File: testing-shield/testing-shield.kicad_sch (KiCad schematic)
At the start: 30 parts, among them J1 I2C Grove, J2 I2C Socket, J3 I2C Header, J4 Side SPI, J5 ISP SPI, J6 UART Header, J7 UART Grove, SW1 UART, SW2 Side SPI, SW3 ISP SPI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

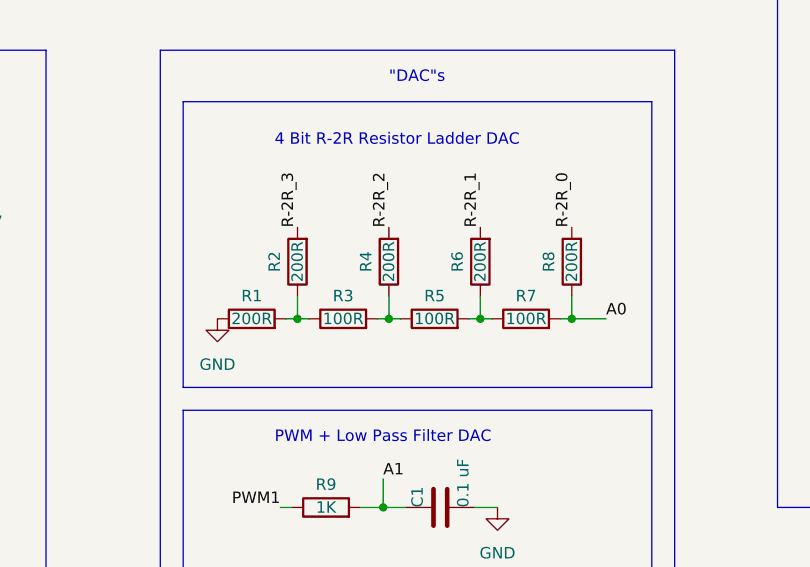
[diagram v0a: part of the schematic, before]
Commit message: testing-shield: Fix R-2R DAC resistor values
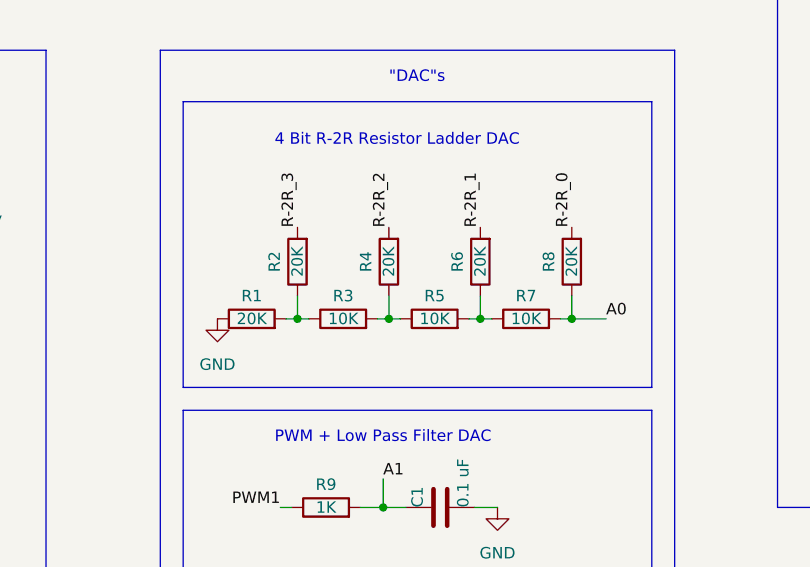
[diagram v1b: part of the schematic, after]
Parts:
- R1, R2, R4, R6, R8: value 200R -> 20K
- R3, R5, R7: value 100R -> 10K
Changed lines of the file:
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@@
       (effects (font (size 1.27 1.27)))
     )
-    (property "Value" "200R" (at 130.81 136.525 90)
+    (property "Value" "20K" (at 130.81 136.525 90)
       (effects (font (size 1.27 1.27)))
     )
@@
       (effects (font (size 1.27 1.27)))
     )
-    (property "Value" "100R" (at 146.05 142.875 90)
+    (property "Value" "10K" (at 146.05 142.875 90)
       (effects (font (size 1.27 1.27)))
     )
@@
       (effects (font (size 1.27 1.27)))
     )
-    (property "Value" "200R" (at 140.97 136.525 90)
+    (property "Value" "20K" (at 140.97 136.525 90)
       (effects (font (size 1.27 1.27)))
     )
@@
       (effects (font (size 1.27 1.27)))
     )
-    (property "Value" "100R" (at 135.89 142.875 90)
+    (property "Value" "10K" (at 135.89 142.875 90)
       (effects (font (size 1.27 1.27)))
     )
@@
       (effects (font (size 1.27 1.27)))
     )
-    (property "Value" "100R" (at 156.21 142.875 90)
+    (property "Value" "10K" (at 156.21 142.875 90)
       (effects (font (size 1.27 1.27)))
     )
@@
       (effects (font (size 1.27 1.27)))
     )
-    (property "Value" "200R" (at 151.13 136.525 90)
+    (property "Value" "20K" (at 151.13 136.525 90)
       (effects (font (size 1.27 1.27)))
     )
@@
       (effects (font (size 1.27 1.27)))
     )
-    (property "Value" "200R" (at 161.29 136.525 90)
+    (property "Value" "20K" (at 161.29 136.525 90)
       (effects (font (size 1.27 1.27)))
     )
@@
       (effects (font (size 1.27 1.27)))
     )
-    (property "Value" "200R" (at 125.73 142.875 90)
-      (effects (font (size 1.27 1.27)))
-    )
+    (property "Value" "20K" (at 125.73 142.875 90)
+      (effects (font (size 1.27 1.27)))
+    )

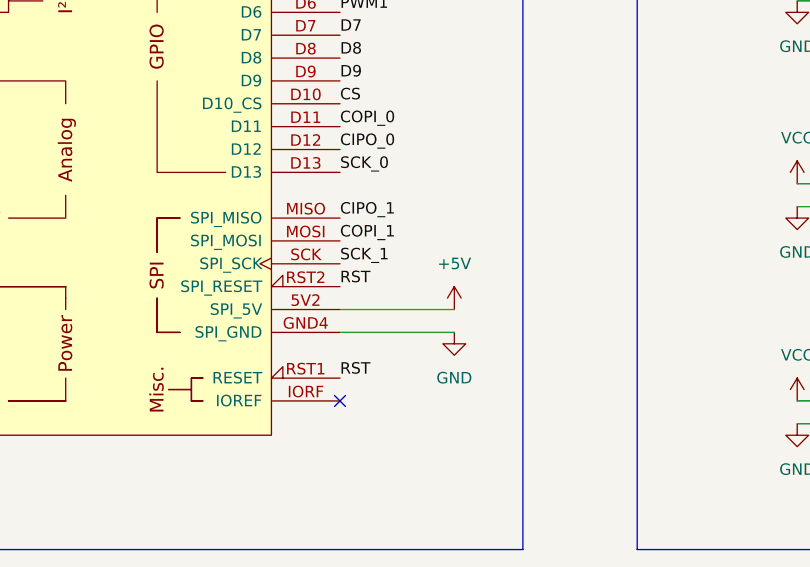
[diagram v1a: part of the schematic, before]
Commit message: testing-shield: do not connect to 5V pin of ISP
Some boards (e.g. the Seeeduino) do not have 5V but VCC there.
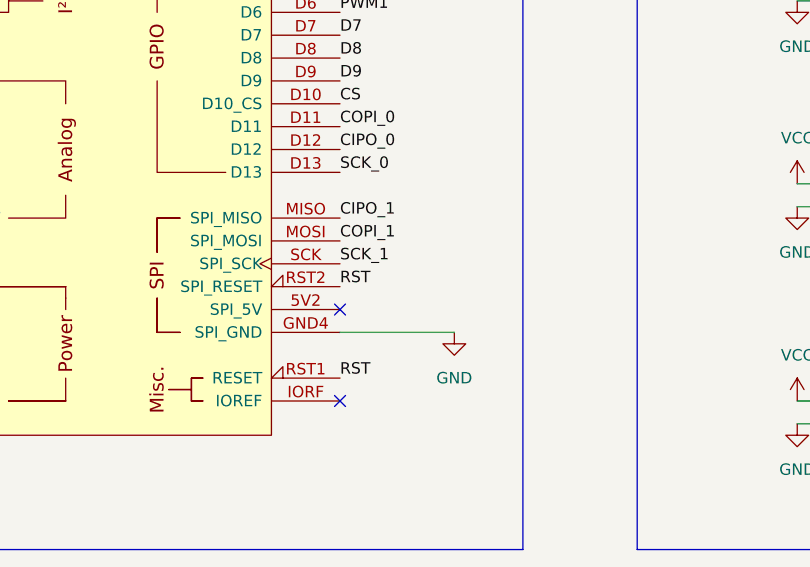
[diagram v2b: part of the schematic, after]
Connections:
- net +5V: no longer XA1.5V2 (SPI_5V)
- no-connect marks 3 -> 4
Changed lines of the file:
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@@
   (junction (at 29.21 85.09) (diameter 0) (color 0 0 0 0)
   )
+  (no_connect (at 82.55 77.47))
   (no_connect (at 31.75 67.31))
   (no_connect (at 82.55 87.63))
@@
   )
   (wire (pts (xy 151.13 142.875) (xy 152.4 142.875))
-    (stroke (width 0) (type default))
-  )
-  (wire (pts (xy 82.55 77.47) (xy 95.25 77.47))
     (stroke (width 0) (type default))
   )
@@
         )
       )
-    )
-  )
-  (symbol (lib_id "power:+5V") (at 95.25 77.47 0) (unit 1)
-    (in_bom yes) (on_board yes) (dnp no) (fields_autoplaced)
-    (property "Reference" "#PWR04" (at 95.25 81.28 0)
-      (effects (font (size 1.27 1.27)) hide)
-    )
-    (property "Value" "+5V" (at 95.25 72.39 0)
-      (effects (font (size 1.27 1.27)))
-    )
-    (property "Footprint" "" (at 95.25 77.47 0)
-      (effects (font (size 1.27 1.27)) hide)
-    )
-    (property "Datasheet" "" (at 95.25 77.47 0)
-      (effects (font (size 1.27 1.27)) hide)
-    )
-    (pin "1")
-    (instances
-      (project "testing-shield"
-        (path "/e57ba8ab-33c5-4264-a7ca-fe36cd423955"
-          (reference "#PWR04") (unit 1)
-        )
-      )

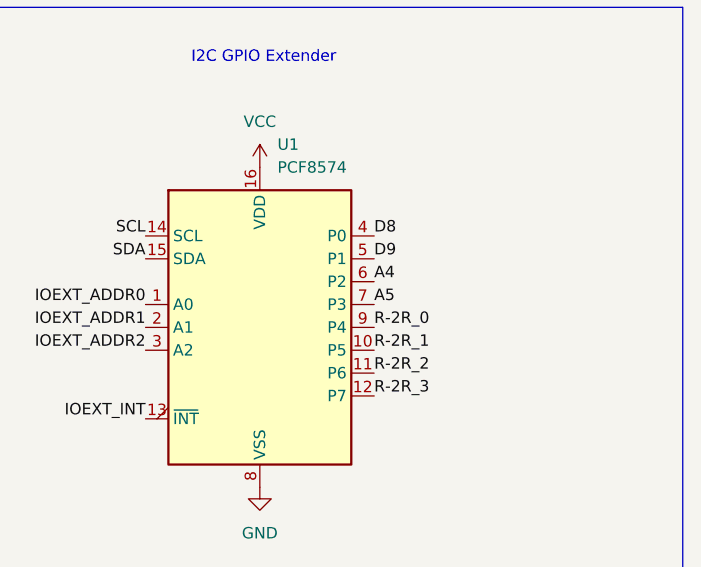
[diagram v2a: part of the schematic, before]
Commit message: testing-shield: connect SCK lines to GPIO extender
This allows reading the SPI clock polarity when the SPI clock is
idle.
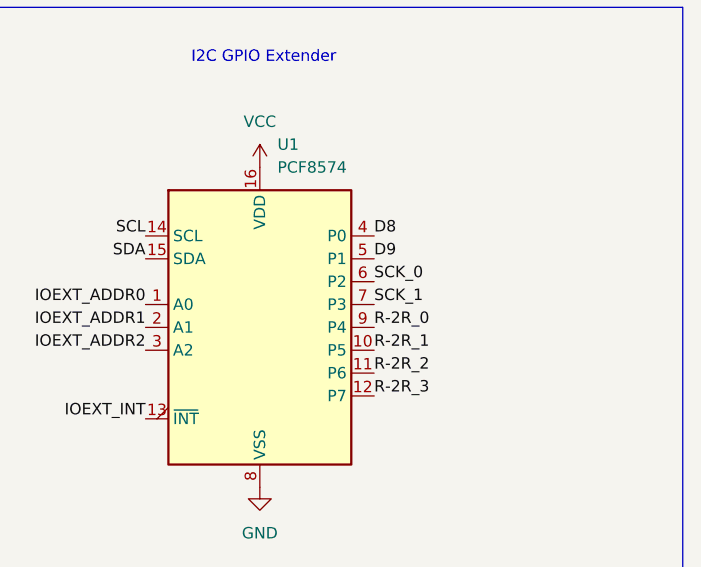
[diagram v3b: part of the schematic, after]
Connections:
- net A4: no longer U1.6 (P2)
- net A5: no longer U1.7 (P3)
- net SCK_0: now also U1.6 (P2)
- net SCK_1: now also U1.7 (P3)
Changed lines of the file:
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@@
     (effects (font (size 1.27 1.27)) (justify left bottom))
   )
-  (label "A5" (at 245.11 101.6 0) (fields_autoplaced)
+  (label "SCK_1" (at 245.11 101.6 0) (fields_autoplaced)
     (effects (font (size 1.27 1.27)) (justify left bottom))
   )
@@
     (effects (font (size 1.27 1.27)) (justify left bottom))
   )
-  (label "A4" (at 245.11 99.06 0) (fields_autoplaced)
+  (label "SCK_0" (at 245.11 99.06 0) (fields_autoplaced)
     (effects (font (size 1.27 1.27)) (justify left bottom))
   )
